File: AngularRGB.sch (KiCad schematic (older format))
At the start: 115 parts, among them SW1 SW_Push, SW1.25U1 MX_1.25U, SW1.25U2 MX_1.25U, SW1.25U3 MX_1.25U, SW1.25U4 MX_1.25U, SW1.25U5 MX_1.25U, SW1.25U6 MX_1.25U, SW1.75U1 MX_1.75U, SW1.75U2 MX_1.75U, SW10 MX_1U, SW11 MX_1U, SW12 MX_1U, SW13 MX_1U, SW14 MX_1U, SW15 MX_1U, SW16 MX_1U, SW17 MX_1U, SW18 MX_1U, SW19 MX_1U, SW2 MX_1U, SW2.25U1 MX_2.25U, SW2.75U1 MX_2.75U, SW20 MX_1U, SW21 MX_1U, SW22 MX_1U, SW23 MX_1U, SW24 MX_1U, SW25 MX_1U, SW26 MX_1U, SW27 MX_1U, SW28 MX_1U, SW29 MX_1U, SW3 MX_1U, SW30 MX_1U, SW31 MX_1U, SW32 MX_1U, SW33 MX_1U, SW4 MX_1U, SW5 MX_1U, SW6 MX_1U, SW7 MX_1U, SW8 MX_1U, SW9 MX_1U, U1 ATmega32U4-MU, U2 USB6B1, Y1 Crystal_GND24

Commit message: Reverse mount WS2812B LED Footprint
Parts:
- LED1: footprint (none) -> MX_Switches:REVERSE_LED
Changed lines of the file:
@@
 EESchema Schematic File Version 4
 LIBS:AngularRGB-cache
-EELAYER 26 0
+EELAYER 29 0
 EELAYER END
 $Descr A4 11693 8268
@@
 F 0 "LED1" H 4700 6425 50  0000 C CNN
 F 1 "WS2812" H 4700 6334 50  0000 C CNN
-F 2 "" H 4700 6150 50  0001 C CNN
+F 2 "MX_Switches:REVERSE_LED" H 4700 6150 50  0001 C CNN
 F 3 "" H 4700 6150 50  0001 C CNN
 	1    4700 6150

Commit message: Led matrix
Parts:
- added LED? (x45): WS2812, MX_Switches:REVERSE_LED, symbol MX_Switches:WS2812
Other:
- moved on the sheet: D1, D10, D11, D12, D13, D14, D15, D16, D17, D18, D19, D2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

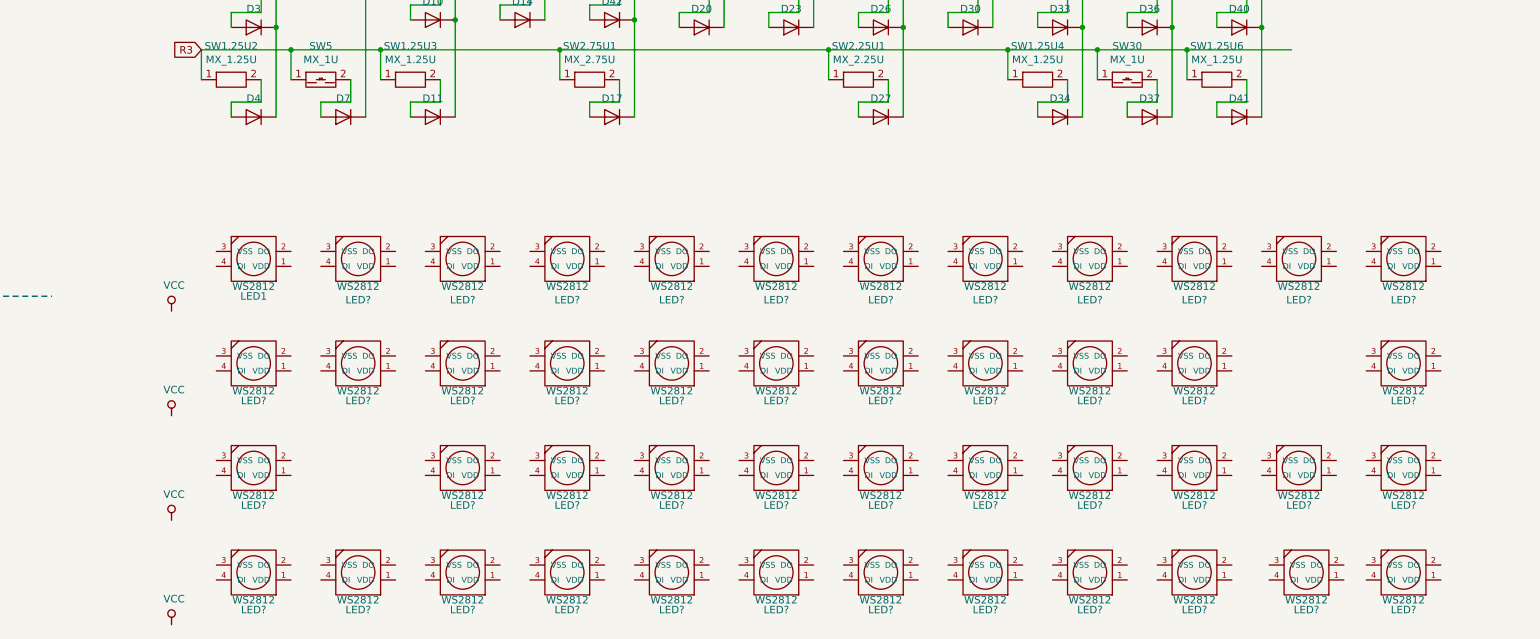
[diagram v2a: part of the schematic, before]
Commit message: LED Matrix Sch
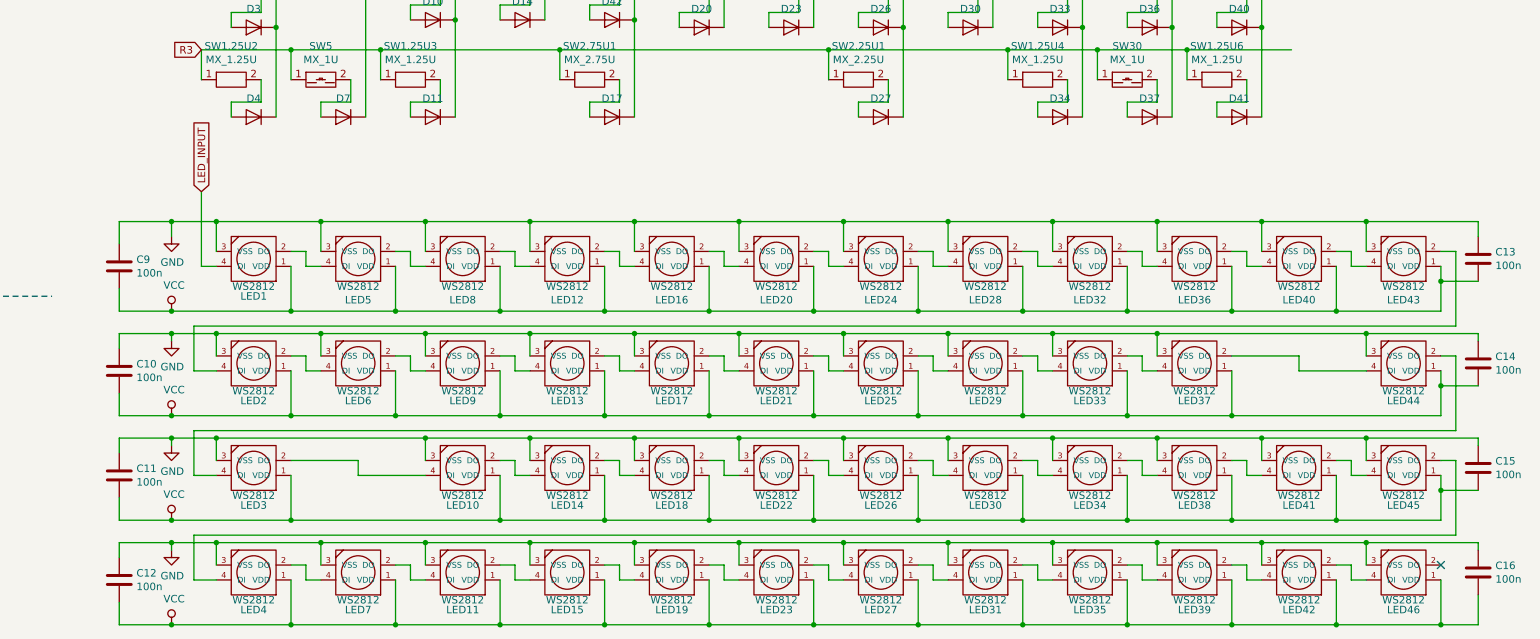
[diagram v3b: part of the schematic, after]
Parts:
- added C10, C11, C12, C13, C14, C15, C16, C9: 100n, symbol Device:C
- gave numbers to parts that had none: 45
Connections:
- net GND: now also LED1.3 (VSS), LED10.3 (VSS), LED11.3 (VSS), LED12.3 (VSS), LED13.3 (VSS), LED14.3 (VSS), LED15.3 (VSS), LED16.3 (VSS), LED17.3 (VSS), LED18.3 (VSS), LED19.3 (VSS), LED2.3 (VSS), LED20.3 (VSS), LED21.3 (VSS), LED22.3 (VSS), LED23.3 (VSS), LED24.3 (VSS), LED25.3 (VSS), LED26.3 (VSS), LED27.3 (VSS), LED28.3 (VSS), LED29.3 (VSS), LED3.3 (VSS), LED30.3 (VSS), LED31.3 (VSS), LED32.3 (VSS), LED33.3 (VSS), LED34.3 (VSS), LED35.3 (VSS), LED36.3 (VSS), LED37.3 (VSS), LED38.3 (VSS), LED39.3 (VSS), LED4.3 (VSS), LED40.3 (VSS), LED41.3 (VSS), LED42.3 (VSS), LED43.3 (VSS), LED44.3 (VSS), LED45.3 (VSS), LED46.3 (VSS), LED5.3 (VSS), LED6.3 (VSS), LED7.3 (VSS), LED8.3 (VSS), LED9.3 (VSS), C10.2, C11.2, C12.2, C13.1, C14.1, C15.1, C16.1, C9.2
- net VCC: now also LED1.1 (VDD), LED10.1 (VDD), LED11.1 (VDD), LED12.1 (VDD), LED13.1 (VDD), LED14.1 (VDD), LED15.1 (VDD), LED16.1 (VDD), LED17.1 (VDD), LED18.1 (VDD), LED19.1 (VDD), LED2.1 (VDD), LED20.1 (VDD), LED21.1 (VDD), LED22.1 (VDD), LED23.1 (VDD), LED24.1 (VDD), LED25.1 (VDD), LED26.1 (VDD), LED27.1 (VDD), LED28.1 (VDD), LED29.1 (VDD), LED3.1 (VDD), LED30.1 (VDD), LED31.1 (VDD), LED32.1 (VDD), LED33.1 (VDD), LED34.1 (VDD), LED35.1 (VDD), LED36.1 (VDD), LED37.1 (VDD), LED38.1 (VDD), LED39.1 (VDD), LED4.1 (VDD), LED40.1 (VDD), LED41.1 (VDD), LED42.1 (VDD), LED43.1 (VDD), LED44.1 (VDD), LED45.1 (VDD), LED46.1 (VDD), LED5.1 (VDD), LED6.1 (VDD), LED7.1 (VDD), LED8.1 (VDD), LED9.1 (VDD), C10.1, C11.1, C12.1, C13.2, C14.2, C15.2, C16.2, C9.1
- net at LED5.2 (DO): now also LED8.4 (DI)
- net at LED5.4 (DI): now also LED1.2 (DO)
- net at LED8.2 (DO): now also LED12.4 (DI)
- net at LED12.2 (DO): now also LED16.4 (DI)
- net at LED16.2 (DO): now also LED20.4 (DI)
- net at LED20.2 (DO): now also LED24.4 (DI)
- net at LED24.2 (DO): now also LED28.4 (DI)
- net LED_INPUT: now reaches LED1.4 (DI)
- net at LED28.2 (DO): now also LED32.4 (DI)
- net at LED32.2 (DO): now also LED36.4 (DI)
- net at LED36.2 (DO): now also LED40.4 (DI)
- net at LED40.2 (DO): now also LED43.4 (DI)
- net at LED43.2 (DO): now also LED2.4 (DI)
- net at LED2.2 (DO): now also LED6.4 (DI)
- net at LED6.2 (DO): now also LED9.4 (DI)
- net at LED9.2 (DO): now also LED13.4 (DI)
- net at LED13.2 (DO): now also LED17.4 (DI)
- net at LED17.2 (DO): now also LED21.4 (DI)
- net at LED21.2 (DO): now also LED25.4 (DI)
- net at LED25.2 (DO): now also LED29.4 (DI)
- net at LED29.2 (DO): now also LED33.4 (DI)
- net at LED33.2 (DO): now also LED37.4 (DI)
- net at LED37.2 (DO): now also LED44.4 (DI)
- net at LED44.2 (DO): now also LED3.4 (DI)
- net at LED3.2 (DO): now also LED10.4 (DI)
- net at LED10.2 (DO): now also LED14.4 (DI)
- net at LED14.2 (DO): now also LED18.4 (DI)
- net at LED18.2 (DO): now also LED22.4 (DI)
- net at LED22.2 (DO): now also LED26.4 (DI)
- net at LED26.2 (DO): now also LED30.4 (DI)
- net at LED30.2 (DO): now also LED34.4 (DI)
- net at LED34.2 (DO): now also LED38.4 (DI)
- net at LED38.2 (DO): now also LED41.4 (DI)
- net at LED41.2 (DO): now also LED45.4 (DI)
- net at LED45.2 (DO): now also LED4.4 (DI)
- net at LED4.2 (DO): now also LED7.4 (DI)
- net at LED7.2 (DO): now also LED11.4 (DI)
- net at LED11.2 (DO): now also LED15.4 (DI)
- net at LED19.2 (DO): now also LED23.4 (DI)
- net at LED19.4 (DI): now also LED15.2 (DO)
- net at LED27.2 (DO): now also LED31.4 (DI)
- net at LED27.4 (DI): now also LED23.2 (DO)
- net at LED46.4 (DI): now also LED42.2 (DO)
- net at LED42.4 (DI): now also LED39.2 (DO)
- net at LED39.4 (DI): now also LED35.2 (DO)
- net at LED31.2 (DO): now also LED35.4 (DI)
- no-connect marks 3 -> 4
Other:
- moved on the sheet: LED42

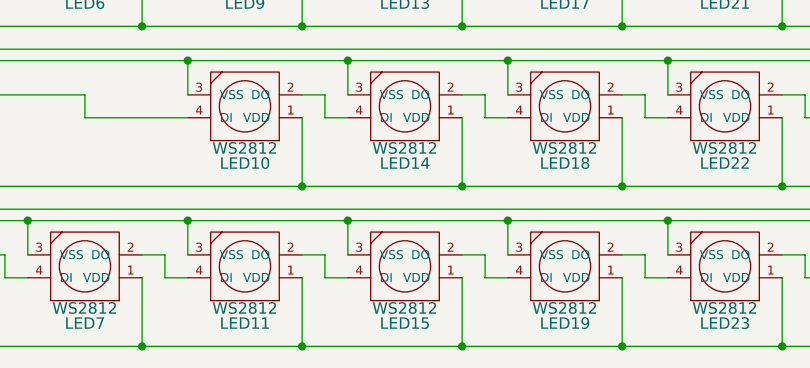
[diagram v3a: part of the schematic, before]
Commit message: LED Matrix Placement
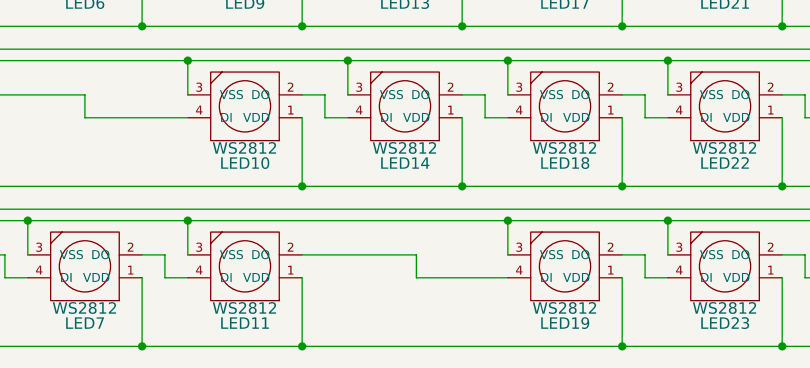
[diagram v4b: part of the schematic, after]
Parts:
- removed LED15: WS2812, MX_Switches:REVERSE_LED, symbol MX_Switches:WS2812
- C10, C11, C12, C13, C14, C15, C16, C9: footprint (none) -> Capacitor_SMD:C_0603_1608Metric
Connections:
- net at LED11.2 (DO): now also LED19.4 (DI)
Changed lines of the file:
@@
-$EndComp
-$Comp
-L MX_Switches:WS2812 LED15
-U 1 1 5D0F0F4A
-P 7850 8650
-F 0 "LED15" H 7850 8900 50  0000 C CNN
-F 1 "WS2812" H 7850 8834 50  0000 C CNN
-F 2 "MX_Switches:REVERSE_LED" H 7850 8650 50  0001 C CNN
-F 3 "" H 7850 8650 50  0001 C CNN
-	1    7850 8650
-	-1   0    0    1
 $EndComp
 $Comp
@@
 	6800 8700 6900 8700
 Wire Wire Line
-	7400 8600 7500 8600
-Wire Wire Line
-	7500 8600 7500 8700
-Wire Wire Line
-	7500 8700 7600 8700
-Wire Wire Line
-	8100 8600 8200 8600
-Wire Wire Line
-	8200 8600 8200 8700
-Wire Wire Line
-	8200 8700 8300 8700
-Wire Wire Line
 	8800 8600 8900 8600
 Wire Wire Line
@@
 	7400 8700 7400 9000
 Connection ~ 7400 9000
-Wire Wire Line
-	7400 9000 8100 9000
-Wire Wire Line
-	8100 8700 8100 9000
-Connection ~ 8100 9000
-Wire Wire Line
-	8100 9000 8800 9000
 Wire Wire Line
 	8800 8700 8800 9000
@@
 	8300 8450 9000 8450
 Wire Wire Line
-	7600 8600 7600 8450
-Connection ~ 7600 8450
-Wire Wire Line
-	7600 8450 8300 8450
-Wire Wire Line
 	6900 8600 6900 8450
 Connection ~ 6900 8450
-Wire Wire Line
-	6900 8450 7600 8450
 Wire Wire Line
 	6200 8600 6200 8450
@@
 F 0 "C9" H 4735 6554 50  0000 R CNN
 F 1 "100n" H 4735 6645 50  0000 R CNN
-F 2 "" H 4888 6450 50  0001 C CNN
+F 2 "Capacitor_SMD:C_0603_1608Metric" H 4888 6450 50  0001 C CNN
 F 3 "~" H 4850 6600 50  0001 C CNN
 	1    4850 6600
@@
 F 0 "C10" H 4735 7254 50  0000 R CNN
 F 1 "100n" H 4735 7345 50  0000 R CNN
-F 2 "" H 4888 7150 50  0001 C CNN
+F 2 "Capacitor_SMD:C_0603_1608Metric" H 4888 7150 50  0001 C CNN
 F 3 "~" H 4850 7300 50  0001 C CNN
 	1    4850 7300
@@
 F 0 "C11" H 4735 7954 50  0000 R CNN
 F 1 "100n" H 4735 8045 50  0000 R CNN
-F 2 "" H 4888 7850 50  0001 C CNN
+F 2 "Capacitor_SMD:C_0603_1608Metric" H 4888 7850 50  0001 C CNN
 F 3 "~" H 4850 8000 50  0001 C CNN
 	1    4850 8000
@@
 F 0 "C12" H 4735 8654 50  0000 R CNN
 F 1 "100n" H 4735 8745 50  0000 R CNN
-F 2 "" H 4888 8550 50  0001 C CNN
+F 2 "Capacitor_SMD:C_0603_1608Metric" H 4888 8550 50  0001 C CNN
 F 3 "~" H 4850 8700 50  0001 C CNN
 	1    4850 8700
@@
 F 0 "C13" H 13835 6596 50  0000 R CNN
 F 1 "100n" H 13835 6505 50  0000 R CNN
-F 2 "" H 13988 6400 50  0001 C CNN
+F 2 "Capacitor_SMD:C_0603_1608Metric" H 13988 6400 50  0001 C CNN
 F 3 "~" H 13950 6550 50  0001 C CNN
 	1    13950 6550
@@
 F 0 "C14" H 13835 7296 50  0000 R CNN
 F 1 "100n" H 13835 7205 50  0000 R CNN
-F 2 "" H 13988 7100 50  0001 C CNN
+F 2 "Capacitor_SMD:C_0603_1608Metric" H 13988 7100 50  0001 C CNN
 F 3 "~" H 13950 7250 50  0001 C CNN
 	1    13950 7250
@@
 F 0 "C15" H 13835 7996 50  0000 R CNN
 F 1 "100n" H 13835 7905 50  0000 R CNN
-F 2 "" H 13988 7800 50  0001 C CNN
+F 2 "Capacitor_SMD:C_0603_1608Metric" H 13988 7800 50  0001 C CNN
 F 3 "~" H 13950 7950 50  0001 C CNN
 	1    13950 7950
@@
 F 0 "C16" H 13835 8696 50  0000 R CNN
 F 1 "100n" H 13835 8605 50  0000 R CNN
-F 2 "" H 13988 8500 50  0001 C CNN
+F 2 "Capacitor_SMD:C_0603_1608Metric" H 13988 8500 50  0001 C CNN
 F 3 "~" H 13950 8650 50  0001 C CNN
 	1    13950 8650
@@
 	13950 6300 13200 6300
 Connection ~ 13200 6300
+Wire Wire Line
+	6900 8450 8300 8450
+Wire Wire Line
+	7400 9000 8800 9000
+Wire Wire Line
+	7400 8600 7900 8600
+Wire Wire Line
+	7900 8600 7900 8700
+Wire Wire Line
+	7900 8700 8300 8700
 $EndSCHEMATC

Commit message: Matrix Connections
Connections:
- net D_P: now reaches R5.2, U2.1 (I/O1)
- net D_N: now reaches R6.2, U2.3 (I/O2)
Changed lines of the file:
@@
 Wire Wire Line
 	7900 8700 8300 8700
+Text Label 6350 1050 0    50   ~ 0
+D_N
+Text Label 6350 2050 0    50   ~ 0
+D_P
 $EndSCHEMATC

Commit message: Finsihed Layout
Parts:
- added J1: Conn_01x09_Male, Connector_PinSocket_2.54mm:PinSocket_1x09_P2.54mm_Vertical, symbol Connector:Conn_01x09_Male
- added TP1, TP2: TestPoint, TestPoint:TestPoint_Pad_D2.0mm, symbol Connector:TestPoint
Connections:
- net C0: now also U1.25 (PD4)
- net C1: now also U1.26 (PD6)
- net C10: now also U1.32 (PC7)
- net C11: now also U1.31 (PC6)
- net C2: now also U1.27 (PD7)
- net C3: now also U1.28 (PB4)
- net C4: now also U1.41 (PF0)
- net C5: now also U1.40 (PF1)
- net C6: now also U1.39 (PF4)
- net C7: now also U1.38 (PF5)
- net C8: now also U1.37 (PF6)
- net C9: now also U1.36 (PF7)
- net GND: now also J1.8 (Pin_8), TP2.1
- net R0: now also U1.22 (PD5)
- net R1: now also U1.21 (PD3)
- net R2: now also U1.20 (PD2)
- net R3: now also U1.12 (PB7)
- net VBUS: now also TP1.1
- net VCC: now also J1.9 (Pin_9)
- net RST: now reaches U1.1 (PE6)
- net RST: now also J1.7 (Pin_7)
- net MOSI: now reaches U1.10 (PB2)
- net MOSI: now also J1.3 (Pin_3)
- net MISO: now reaches U1.11 (PB3)
- net MISO: now also J1.2 (Pin_2)
- net SCL: now reaches U1.18 (PD0)
- net SDA: now reaches U1.19 (PD1)
- net CS: now reaches U1.29 (PB5)
- net CS: now also J1.4 (Pin_4)
- net IRQ: now reaches U1.30 (PB6)
- net IRQ: now also J1.5 (Pin_5)
- net SS: now reaches U1.8 (PB0)
- net SCK: now reaches U1.9 (PB1)
- net SCK: now also J1.1 (Pin_1)
- no-connect marks 4 -> 5
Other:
- moved on the sheet: SW1.25U1
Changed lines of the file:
@@
 EESchema Schematic File Version 4
 LIBS:AngularRGB-cache
-EELAYER 29 0
+EELAYER 26 0
 EELAYER END
 $Descr A3 16535 11693
@@
 F 3 "" H 5600 4150 50  0001 C CNN
 	1    5600 4150
-	1    0    0    -1
+	0    1    1    0
 $EndComp
 $Comp
@@
 	12400 3700 12400 3550
 Wire Wire Line
-	5600 4400 5600 4300
+	5600 4400 5600 4350
 Wire Wire Line
 	5600 4300 5800 4300
@@
 	12000 3250 12700 3250
 Wire Wire Line
-	5400 3950 6000 3950
+	5400 3950 5600 3950
 Text GLabel 5400 3950 0    50   Input ~ 0
 R1
@@
 Wire Wire Line
 	5850 1000 5850 800
-Wire Wire Line
-	5850 800  6050 800
 Connection ~ 5600 1000
 Wire Wire Line
@@
 Wire Wire Line
 	6800 1550 6800 1600
-Text Label 5900 800  2    50   ~ 0
+Text Label 5850 1000 2    50   ~ 0
 VBUS
 Text Label 1700 4250 2    50   ~ 0
@@
 Text Label 6350 2050 0    50   ~ 0
 D_P
+Connection ~ 5600 3950
+Wire Wire Line
+	5600 3950 6000 3950
+Connection ~ 5600 4350
+Wire Wire Line
+	5600 4350 5600 4300
+Text Label 3100 3250 0    50   ~ 0
+MISO
+Text Label 3100 3150 0    50   ~ 0
+MOSI
+Text Label 3100 3050 0    50   ~ 0
+SCK
+Text Label 3100 2950 0    50   ~ 0
+SS
+Text Label 3100 4150 0    50   ~ 0
+SCL
+Text Label 3100 4250 0    50   ~ 0
+SDA
+Text GLabel 3100 4650 2    50   Input ~ 0
+R0
+Text GLabel 3100 4450 2    50   Input ~ 0
+R1
+Text GLabel 3100 4350 2    50   Input ~ 0
+R2
+Text GLabel 3100 3650 2    50   Input ~ 0
+R3
+Text GLabel 3300 4550 2    50   Input ~ 0
+C0
+Wire Wire Line
+	3300 4550 3100 4550
+Text GLabel 3300 4750 2    50   Input ~ 0
+C1
+Wire Wire Line
+	3300 4750 3100 4750
+Text GLabel 3300 4850 2    50   Input ~ 0
+C2
+Wire Wire Line
+	3300 4850 3100 4850
+Text GLabel 3300 3350 2    50   Input ~ 0
+C3
+Wire Wire Line
+	3300 3350 3100 3350
+Text GLabel 3200 5350 2    50   Input ~ 0
+C4
+Wire Wire Line
+	3200 5350 3100 5350
+Text GLabel 3200 5450 2    50   Input ~ 0
+C5
+Wire Wire Line
+	3200 5450 3100 5450
+Text GLabel 3200 5550 2    50   Input ~ 0
+C6
+Wire Wire Line
+	3200 5550 3100 5550
+Text GLabel 3200 5650 2    50   Input ~ 0
+C7
+Wire Wire Line
+	3200 5650 3100 5650
+Text GLabel 3200 5750 2    50   Input ~ 0
+C8
+Wire Wire Line
+	3200 5750 3100 5750
+Text GLabel 3200 5850 2    50   Input ~ 0
+C9
+Wire Wire Line
+	3200 5850 3100 5850
+Text GLabel 3300 3950 2    50   Input ~ 0
+C10
+Wire Wire Line
+	3300 3950 3100 3950
+Text GLabel 3300 3850 2    50   Input ~ 0
+C11
+Wire Wire Line
+	3300 3850 3100 3850
+Text Label 3100 5150 0    50   ~ 0
+RST
+Text Label 3100 3450 0    50   ~ 0
+CS
+Text Label 3100 3550 0    50   ~ 0
+IRQ
+$Comp
+L Connector:Conn_01x09_Male J1
+U 1 1 5D92FC0C
+P 1050 7750
+F 0 "J1" H 1150 8400 50  0000 C CNN
+F 1 "Conn_01x09_Male" H 1150 8300 50  0000 C CNN
+F 2 "Connector_PinSocket_2.54mm:PinSocket_1x09_P2.54mm_Vertical" H 1050 7750 50  0001 C CNN
+F 3 "~" H 1050 7750 50  0001 C CNN
+	1    1050 7750
+	1    0    0    -1
+$EndComp
+$Comp
+L power:VCC #PWR0103
+U 1 1 5D9327D7
+P 1300 8200
+F 0 "#PWR0103" H 1300 8050 50  0001 C CNN
+F 1 "VCC" H 1318 8373 50  0000 C CNN
+F 2 "" H 1300 8200 50  0001 C CNN
+F 3 "" H 1300 8200 50  0001 C CNN
+	1    1300 8200
+	-1   0    0    1
+$EndComp
+$Comp
+L power:GND #PWR0104
+U 1 1 5D9BC09D
+P 1450 8200
+F 0 "#PWR0104" H 1450 7950 50  0001 C CNN
+F 1 "GND" H 1455 8027 50  0000 C CNN
+F 2 "" H 1450 8200 50  0001 C CNN
+F 3 "" H 1450 8200 50  0001 C CNN
+	1    1450 8200
+	1    0    0    -1
+$EndComp
+Wire Wire Line
+	1250 8150 1300 8150
+Wire Wire Line
+	1300 8150 1300 8200
+Wire Wire Line
+	1450 8200 1450 8050
+Wire Wire Line
+	1450 8050 1250 8050
+Text Label 1250 7950 0    50   ~ 0
+RST
+NoConn ~ 1250 7850
+Text Label 1250 7750 0    50   ~ 0
+IRQ
+Text Label 1250 7650 0    50   ~ 0
+CS
+Text Label 1250 7550 0    50   ~ 0
+MOSI
+Text Label 1250 7450 0    50   ~ 0
+MISO
+Text Label 1250 7350 0    50   ~ 0
+SCK
+$Comp
+L Connector:TestPoint TP1
+U 1 1 5DE0D40F
+P 5700 700
+F 0 "TP1" H 5758 820 50  0000 L CNN
+F 1 "TestPoint" H 5758 729 50  0000 L CNN
+F 2 "TestPoint:TestPoint_Pad_D2.0mm" H 5900 700 50  0001 C CNN
+F 3 "~" H 5900 700 50  0001 C CNN
+	1    5700 700
+	1    0    0    -1
+$EndComp
+Wire Wire Line
+	6050 800  5850 800
+Wire Wire Line
+	5850 800  5700 800
+Wire Wire Line
+	5700 800  5700 700
+Connection ~ 5850 800
+$Comp
+L Connector:TestPoint TP2
+U 1 1 5E039B7F
+P 7150 700
+F 0 "TP2" H 7208 820 50  0000 L CNN
+F 1 "TestPoint" H 7208 729 50  0000 L CNN
+F 2 "TestPoint:TestPoint_Pad_D2.0mm" H 7350 700 50  0001 C CNN
+F 3 "~" H 7350 700 50  0001 C CNN
+	1    7150 700
+	1    0    0    -1
+$EndComp
+$Comp
+L power:GND #PWR022
+U 1 1 5E039D40
+P 7150 700
+F 0 "#PWR022" H 7150 450 50  0001 C CNN
+F 1 "GND" H 7155 527 50  0000 C CNN
+F 2 "" H 7150 700 50  0001 C CNN
+F 3 "" H 7150 700 50  0001 C CNN
+	1    7150 700
+	1    0    0    -1
+$EndComp
 $EndSCHEMATC

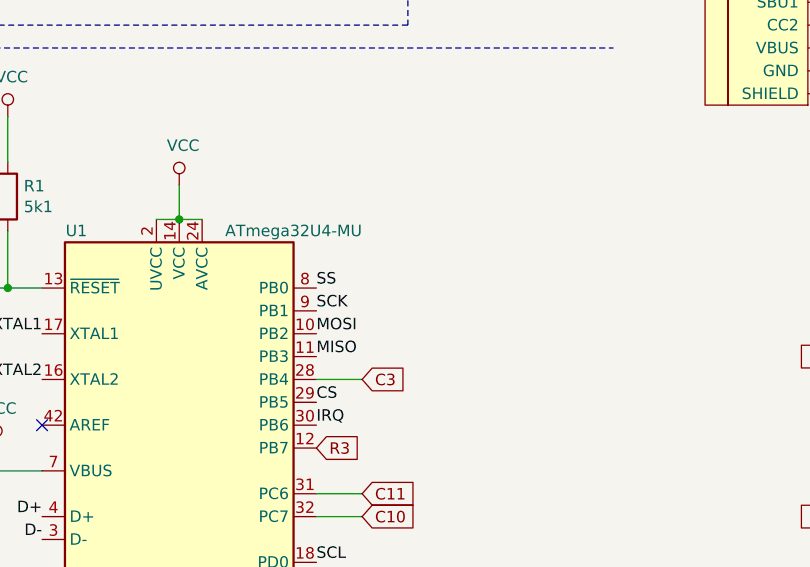
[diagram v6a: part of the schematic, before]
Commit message: Fixed LED Input
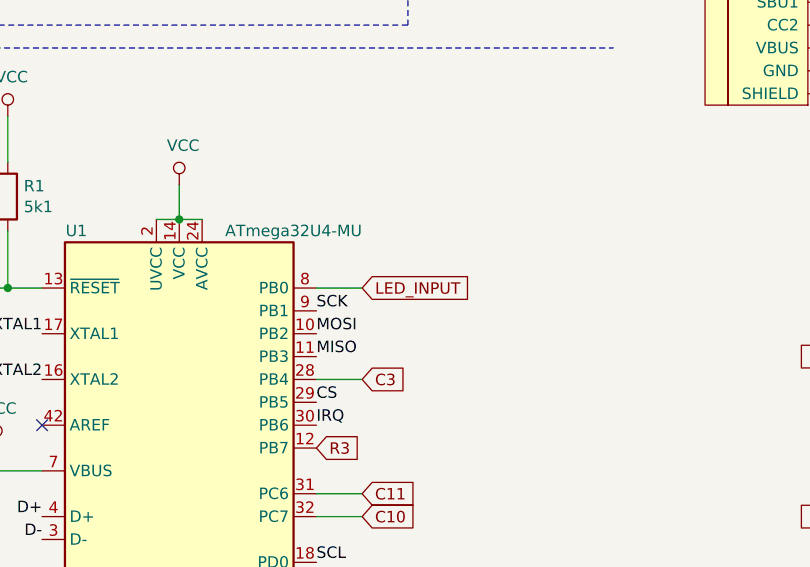
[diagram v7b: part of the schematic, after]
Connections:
- net SS is gone; now on net LED_INPUT: U1.8 (PB0)
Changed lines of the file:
@@
 EESchema Schematic File Version 4
-LIBS:AngularRGB-cache
 EELAYER 26 0
 EELAYER END
@@
 Text Label 3100 3050 0    50   ~ 0
 SCK
-Text Label 3100 2950 0    50   ~ 0
-SS
 Text Label 3100 4150 0    50   ~ 0
 SCL
@@
 Text Label 3100 5150 0    50   ~ 0
 RST
-Text Label 3100 3450 0    50   ~ 0
-CS
 Text Label 3100 3550 0    50   ~ 0
 IRQ
@@
 	1    0    0    -1
 $EndComp
+Text Label 3100 3450 0    50   ~ 0
+CS
+Text GLabel 3300 2950 2    50   Input ~ 0
+LED_INPUT
+Wire Wire Line
+	3300 2950 3100 2950
 $EndSCHEMATC
